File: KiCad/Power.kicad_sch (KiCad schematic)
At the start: 34 parts, among them SW4 SW_DPST, U10 TL074, U2 TL074, U3 TL074, U4 40106, U5 TL074, U6 TL074, U7 TL074, U8 TL074, U9 TL074

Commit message: added osc core and tuning to pcb layout
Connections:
- net +9V: now also SW4.2; no longer SW4.4
- net -9V: now also SW4.4; no longer SW4.2
- net GND: now also U5.10 (+); no longer U5.12 (+)
- net at SW4.1: now also B1.1; no longer B2.2
- net at SW4.3: now also B2.2; no longer B1.1
- new net: U5.8, U5.9 (-)
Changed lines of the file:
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@@
 		(lib_id "Amplifier_Operational:TL074")
 		(at 120.65 105.41 0)
-		(unit 4)
+		(unit 3)
 		(body_style 1)
 		(exclude_from_sim no)
@@
 				(path "/3ca3a63e-46c1-4b14-be30-fce478aad491"
 					(reference "U5")
-					(unit 4)
+					(unit 3)
 				)
 			)
@@
 		(lib_id "Switch:SW_DPST")
 		(at 97.79 38.1 0)
+		(mirror x)
 		(unit 1)
 		(body_style 1)
@@
 		(in_pos_files yes)
 		(dnp no)
-		(fields_autoplaced yes)
 		(property "Reference" "SW4"
-			(at 97.79 31.75 0)
+			(at 97.79 44.45 0)
 			(show_name no)
 			(do_not_autoplace no)
@@
 		)
 		(property "Value" "SW_DPST"
-			(at 97.79 31.75 0)
-			(hide yes)
-			(show_name no)
+			(at 97.79 44.45 0)
+			(hide yes)
+			(show_name no)

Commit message: minor but important changes to schematic
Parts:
- added C30, C31: 0.1u, Capacitor_SMD:C_0201_0603Metric, symbol Device:C_Small
- added U11: TL074, Package_DIP:DIP-14_W7.62mm, symbol Amplifier_Operational:TL074
- added unit 4 of U2
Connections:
- net +5V: now also U11.1, U11.2 (-); no longer R72.1, R74.2
- net +9V: now also C30.1, U11.4 (V+)
- net -5V: now also U11.13 (-), U11.14; no longer R71.1, R73.2
- net -9V: now also C31.2, U11.11 (V-)
- net GND: now also C30.2, C31.1, U11.10 (+), U2.12 (+)
- net Thaw 5: now reaches U5.8, U5.9 (-)
- net Thaw 8: now reaches U8.13 (-), U8.14
- net Thaw 7: now reaches U7.13 (-), U7.14
- net Thaw 3: now reaches U3.13 (-), U3.14
- new net: R72.1, R74.2, U11.3 (+)
- new net: R71.1, R73.2, U11.12 (+)
- new net Thaw 11: U11.8, U11.9 (-)
- new net Thaw 2: U2.13 (-), U2.14
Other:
- moved on the sheet: R71, R73, U3D, U5C, U7D, U8D

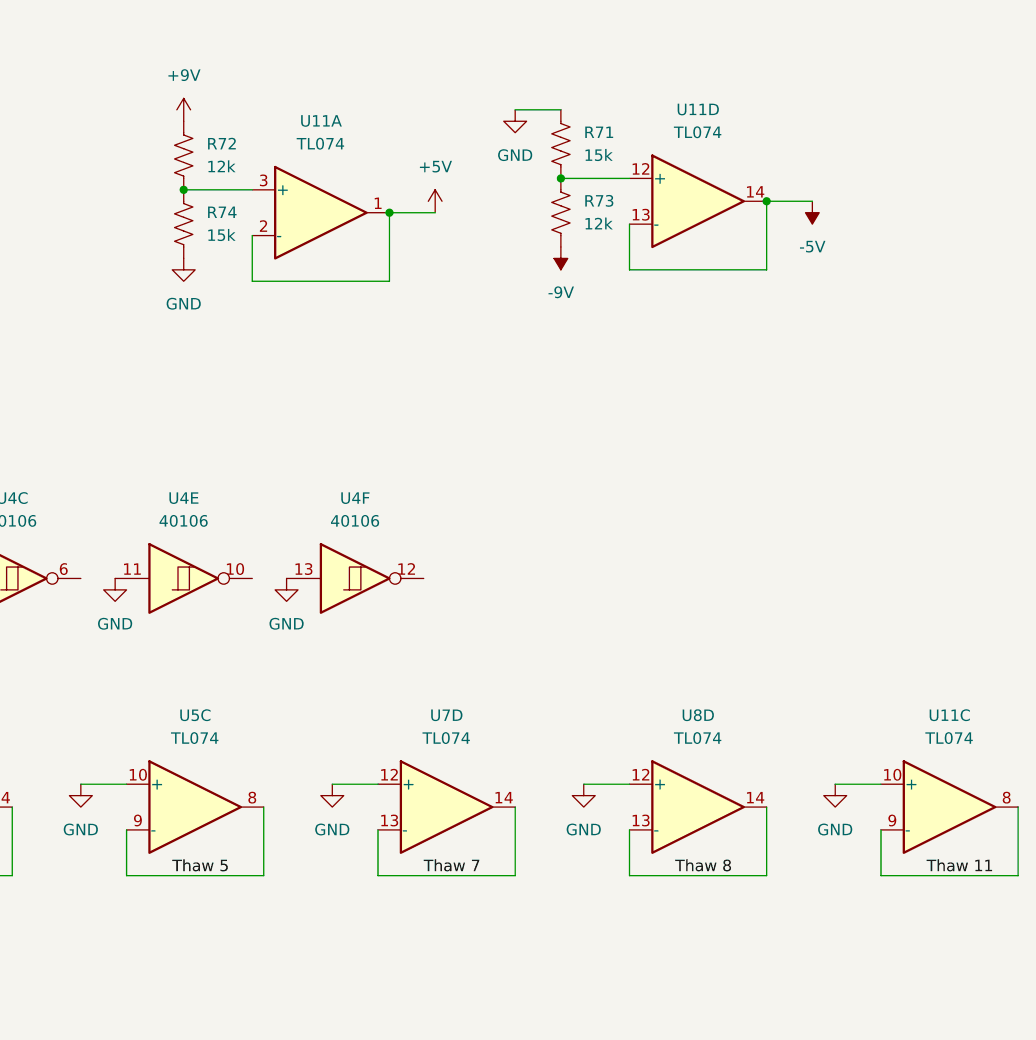
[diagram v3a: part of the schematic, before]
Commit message: fixed custom pot voltage control schematic
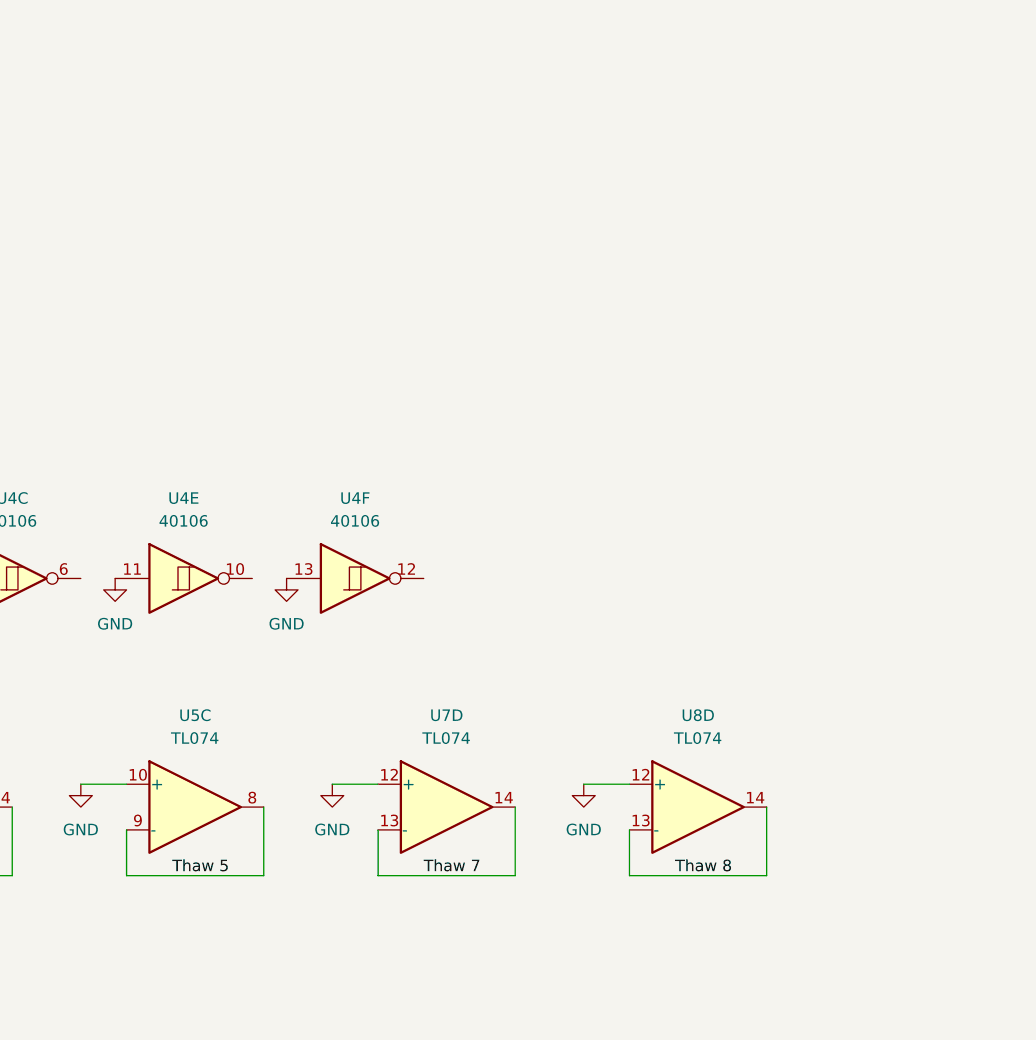
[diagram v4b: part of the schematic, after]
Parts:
- removed R71, R74: 15k, Resistor_SMD:R_0201_0603Metric, symbol Device:R_US
- removed R72, R73: 12k, Resistor_SMD:R_0201_0603Metric, symbol Device:R_US
- removed unit 3 of U11
- removed unit 4 of U11
- removed unit 1 of U11

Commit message: routed oscillator
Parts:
- renumbered U7 to U5
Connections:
- net Thaw 5 renamed Thaw 5C
- net Thaw 7 renamed Thaw 5D
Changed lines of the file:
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@@
 		)
 	)
-	(label "Thaw 5"
+	(label "Thaw 5C"
 		(at 130.81 113.03 0)
 		(effects
@@
 		)
 	)
-	(label "Thaw 7"
+	(label "Thaw 5D"
 		(at 158.75 113.03 0)
 		(effects
@@
 		(dnp no)
 		(fields_autoplaced yes)
-		(property "Reference" "U7"
+		(property "Reference" "U5"
 			(at 161.29 95.25 0)
 			(show_name no)
@@
 			(project "Electronic Trombone"
 				(path "/3ca3a63e-46c1-4b14-be30-fce478aad491"
-					(reference "U7")
+					(reference "U5")
 					(unit 4)
 				)

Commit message: routed the filter, updated 0201 footprints to 0402
JLCPCB's economy PCBA has a footprint bottom limit of 0402 imperial
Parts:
- C12, C13, C14, C15, C16, C17, C18, C19, C20, C21, C22, C23, C24, C25, C26, C27, C28, C29, C30, C31: footprint Capacitor_SMD:C_0201_0603Metric -> Capacitor_SMD:C_0402_1005Metric
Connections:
- net GND: now also U8.3 (+); no longer U8.12 (+)
- net Thaw 8: now also U8.1, U8.2 (-); no longer U8.13 (-), U8.14
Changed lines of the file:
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@@
 			)
 		)
-		(property "Footprint" "Capacitor_SMD:C_0201_0603Metric"
+		(property "Footprint" "Capacitor_SMD:C_0402_1005Metric"
 			(at 50.8 110.49 0)
 			(hide yes)
@@
 			)
 		)
-		(property "Footprint" "Capacitor_SMD:C_0201_0603Metric"
+		(property "Footprint" "Capacitor_SMD:C_0402_1005Metric"
 			(at 22.86 44.45 0)
 			(hide yes)
@@
 			)
 		)
-		(property "Footprint" "Capacitor_SMD:C_0201_0603Metric"
+		(property "Footprint" "Capacitor_SMD:C_0402_1005Metric"
 			(at 55.88 67.31 0)
 			(hide yes)
@@
 			)
 		)
-		(property "Footprint" "Capacitor_SMD:C_0201_0603Metric"
+		(property "Footprint" "Capacitor_SMD:C_0402_1005Metric"
 			(at 50.8 187.96 0)
 			(hide yes)
@@
 			)
 		)
-		(property "Footprint" "Capacitor_SMD:C_0201_0603Metric"
+		(property "Footprint" "Capacitor_SMD:C_0402_1005Metric"
 			(at 50.8 132.08 0)
 			(hide yes)
@@
 		(lib_id "Amplifier_Operational:TL074")
 		(at 189.23 105.41 0)
-		(unit 4)
+		(unit 1)
 		(body_style 1)
 		(exclude_from_sim no)
@@
 				(path "/3ca3a63e-46c1-4b14-be30-fce478aad491"
 					(reference "U8")
-					(unit 4)
+					(unit 1)
 				)
 			)
@@
 			)
 		)
-		(property "Footprint" "Capacitor_SMD:C_0201_0603Metric"
+		(property "Footprint" "Capacitor_SMD:C_0402_1005Metric"
 			(at 96.52 187.96 0)
 			(hide yes)
@@
 			)
 		)
-		(property "Footprint" "Capacitor_SMD:C_0201_0603Metric"
+		(property "Footprint" "Capacitor_SMD:C_0402_1005Metric"
 			(at 22.86 110.49 0)
 			(hide yes)
@@
 			)
 		)
-		(property "Footprint" "Capacitor_SMD:C_0201_0603Metric"
+		(property "Footprint" "Capacitor_SMD:C_0402_1005Metric"
 			(at 50.8 151.13 0)
 			(hide yes)
@@
 			)
 		)
-		(property "Footprint" "Capacitor_SMD:C_0201_0603Metric"
+		(property "Footprint" "Capacitor_SMD:C_0402_1005Metric"
 			(at 17.78 67.31 0)
 			(hide yes)
@@
 			)
 		)
-		(property "Footprint" "Capacitor_SMD:C_0201_0603Metric"
+		(property "Footprint" "Capacitor_SMD:C_0402_1005Metric"
 			(at 22.86 132.08 0)
 			(hide yes)
@@
 			)
 		)
-		(property "Footprint" "Capacitor_SMD:C_0201_0603Metric"
+		(property "Footprint" "Capacitor_SMD:C_0402_1005Metric"
 			(at 50.8 168.91 0)
 			(hide yes)
@@
 			)
 		)
-		(property "Footprint" "Capacitor_SMD:C_0201_0603Metric"
+		(property "Footprint" "Capacitor_SMD:C_0402_1005Metric"
 			(at 22.86 187.96 0)
 			(hide yes)
@@
 			)
 		)
-		(property "Footprint" "Capacitor_SMD:C_0201_0603Metric"
+		(property "Footprint" "Capacitor_SMD:C_0402_1005Metric"
 			(at 22.86 25.4 0)
 			(hide yes)
@@
 			)
 		)
-		(property "Footprint" "Capacitor_SMD:C_0201_0603Metric"
+		(property "Footprint" "Capacitor_SMD:C_0402_1005Metric"
 			(at 22.86 151.13 0)
 			(hide yes)
@@
 			)
 		)
-		(property "Footprint" "Capacitor_SMD:C_0201_0603Metric"
+		(property "Footprint" "Capacitor_SMD:C_0402_1005Metric"
 			(at 68.58 187.96 0)
 			(hide yes)
@@
 			)
 		)
-		(property "Footprint" "Capacitor_SMD:C_0201_0603Metric"
+		(property "Footprint" "Capacitor_SMD:C_0402_1005Metric"
 			(at 50.8 90.17 0)
 			(hide yes)
@@
 			)
 		)
-		(property "Footprint" "Capacitor_SMD:C_0201_0603Metric"
+		(property "Footprint" "Capacitor_SMD:C_0402_1005Metric"
 			(at 22.86 168.91 0)
 			(hide yes)
@@
 			)
 		)
-		(property "Footprint" "Capacitor_SMD:C_0201_0603Metric"
+		(property "Footprint" "Capacitor_SMD:C_0402_1005Metric"
 			(at 50.8 44.45 0)
 			(hide yes)
@@
 			)
 		)
-		(property "Footprint" "Capacitor_SMD:C_0201_0603Metric"
+		(property "Footprint" "Capacitor_SMD:C_0402_1005Metric"
 			(at 50.8 25.4 0)
 			(hide yes)
@@
 			)
 		)
-		(property "Footprint" "Capacitor_SMD:C_0201_0603Metric"
+		(property "Footprint" "Capacitor_SMD:C_0402_1005Metric"
 			(at 22.86 90.17 0)
 			(hide yes)

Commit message: amplifier layout and routing
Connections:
- net GND: now also U2.3 (+); no longer U2.12 (+)
- net Thaw 2: now also U2.1, U2.2 (-); no longer U2.13 (-), U2.14
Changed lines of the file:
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@@
 		(lib_id "Amplifier_Operational:TL074")
 		(at 77.47 105.41 0)
-		(unit 4)
+		(unit 1)
 		(body_style 1)
 		(exclude_from_sim no)
@@
 				(path "/3ca3a63e-46c1-4b14-be30-fce478aad491"
 					(reference "U2")
-					(unit 4)
+					(unit 1)
 				)
 			)

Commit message: placed and routed envelope core
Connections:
- net GND: now also U3.5 (+); no longer U3.12 (+)
- net Thaw 3: now also U3.6 (-), U3.7; no longer U3.13 (-), U3.14
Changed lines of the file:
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@@
 		(lib_id "Amplifier_Operational:TL074")
 		(at 105.41 105.41 0)
-		(unit 4)
+		(unit 2)
 		(body_style 1)
 		(exclude_from_sim no)
@@
 				(path "/3ca3a63e-46c1-4b14-be30-fce478aad491"
 					(reference "U3")
-					(unit 4)
+					(unit 2)
 				)
 			)
